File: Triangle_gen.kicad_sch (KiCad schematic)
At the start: 10 parts, among them U42 OPA2197xDGK

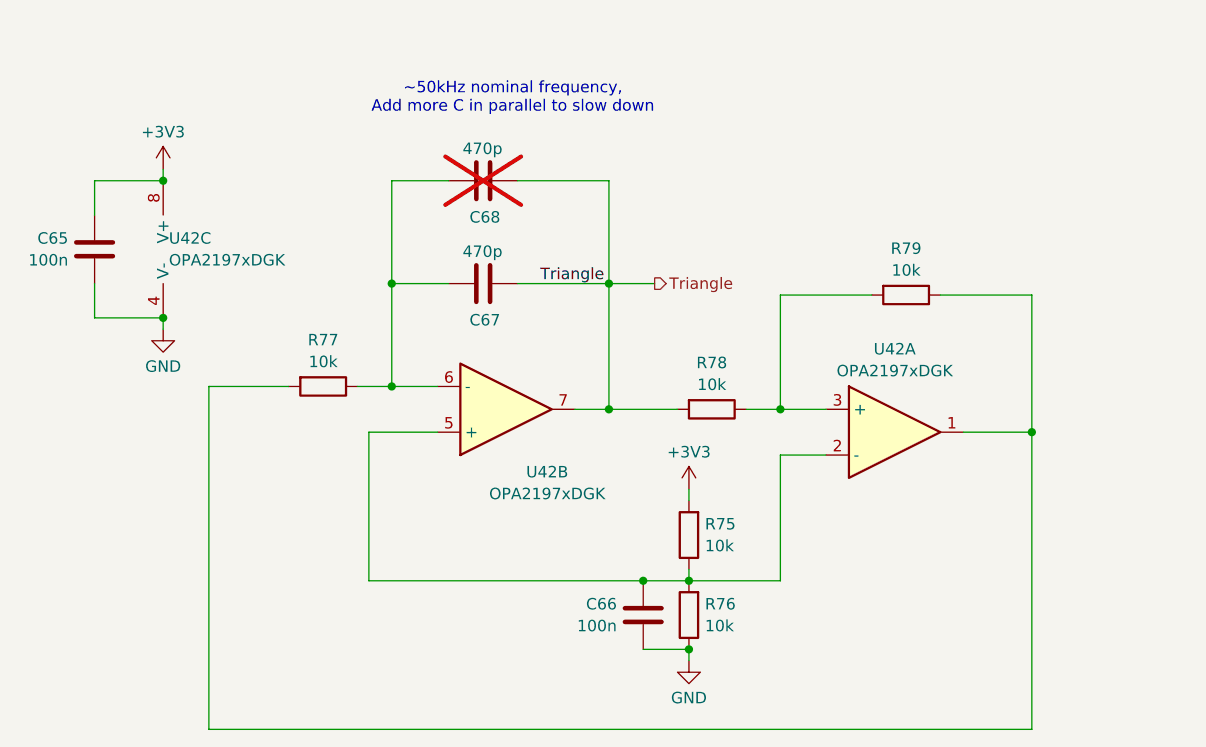
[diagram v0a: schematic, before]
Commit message: 8ch layout applied, connectors aligned to nucleo
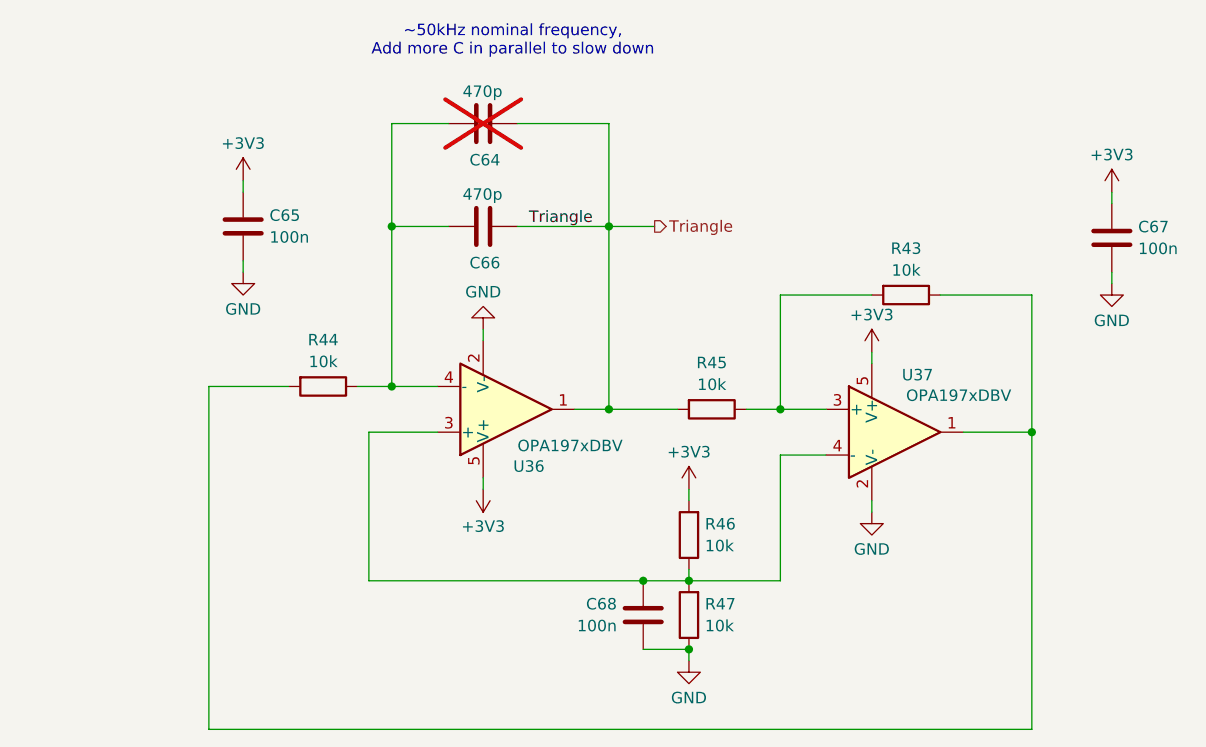
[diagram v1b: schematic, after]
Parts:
- removed U42: OPA2197xDGK, Package_SO:VSSOP-8_3x3mm_P0.65mm, symbol Amplifier_Operational:OPA2197xDGK
- added C67: 100n, Capacitor_SMD:C_0603_1608Metric, symbol Device:C
- added U36, U37: OPA197xDBV, Package_TO_SOT_SMD:SOT-23-5, symbol Amplifier_Operational:OPA197xDBV
- C64: renamed from C68; footprint Capacitor_SMD:C_0805_2012Metric -> Capacitor_SMD:C_0603_1608Metric; LCSC C1743 -> C1620
- C65: footprint Capacitor_SMD:C_0805_2012Metric -> Capacitor_SMD:C_0603_1608Metric; LCSC C28233 -> C14663
- C66: renamed from C67; footprint Capacitor_SMD:C_0805_2012Metric -> Capacitor_SMD:C_0603_1608Metric; LCSC C1743 -> C1620
- C68: renamed from C66; footprint Capacitor_SMD:C_0805_2012Metric -> Capacitor_SMD:C_0603_1608Metric; LCSC C28233 -> C14663
- R43: renamed from R79; footprint Resistor_SMD:R_0805_2012Metric -> Resistor_SMD:R_0603_1608Metric; LCSC C17414 -> C25804
- R44: renamed from R77; footprint Resistor_SMD:R_0805_2012Metric -> Resistor_SMD:R_0603_1608Metric; LCSC C17414 -> C25804
- R45: renamed from R78; footprint Resistor_SMD:R_0805_2012Metric -> Resistor_SMD:R_0603_1608Metric; LCSC C17414 -> C25804
- R46: renamed from R75; footprint Resistor_SMD:R_0805_2012Metric -> Resistor_SMD:R_0603_1608Metric; LCSC C17414 -> C25804
- R47: renamed from R76; footprint Resistor_SMD:R_0805_2012Metric -> Resistor_SMD:R_0603_1608Metric; LCSC C17414 -> C25804
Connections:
- net +3V3: now also C67.1, U36.5 (V+), U37.5 (V+)
- net GND: now also C67.2, U36.2 (V-), U37.2 (V-)
- net Triangle: now also U36.1
- net at R43.1, R44.2: now also U37.1
- net at C68.1, R46.1, R47.2: now also U36.3 (+), U37.4 (-)
- net at R43.2, R45.1: now also U37.3 (+)
- net at C64.2, C66.2, R44.1: now also U36.4 (-)
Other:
- moved on the sheet: C64, C66
